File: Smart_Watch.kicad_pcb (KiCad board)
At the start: 4 copper layers, 32 x 32 mm, 59 parts, among them J2 Conn_01x02, J3 Conn_01x06, J4 Conn_01x02, J5 USB_C_Receptacle_USB2.0_16P, SW2 SW_Push, SW3 SW_Push, SW4 SW_Push, SW5 SW_Push, SW6 SW_Push, SW7 SW_Push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

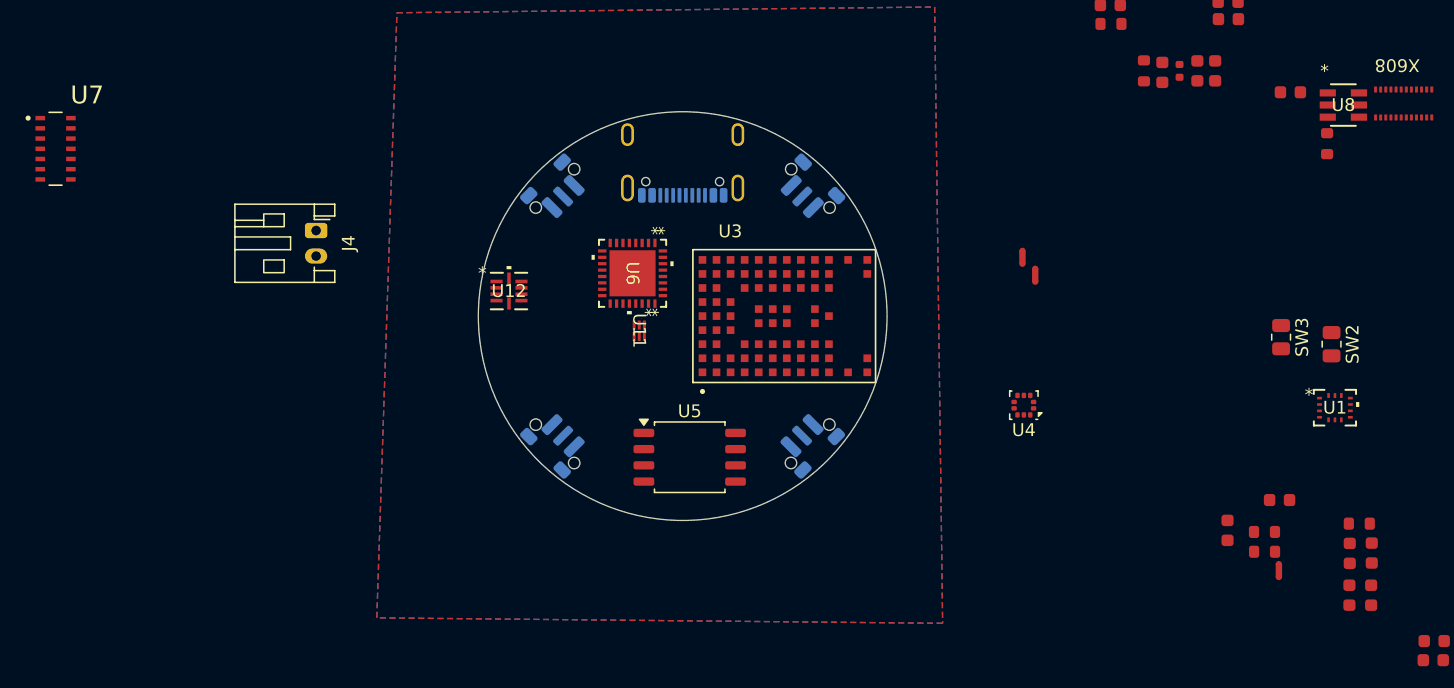
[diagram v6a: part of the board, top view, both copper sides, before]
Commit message: Remove heart rate sensor from main board
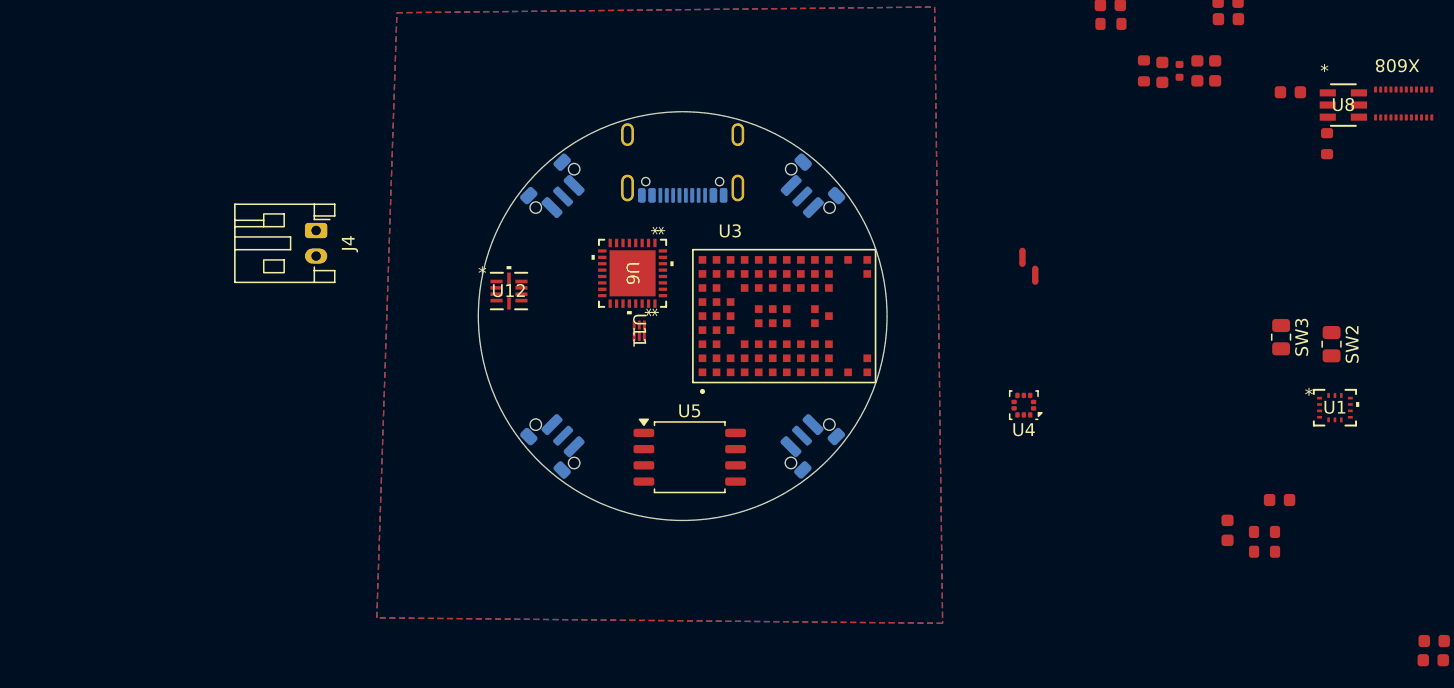
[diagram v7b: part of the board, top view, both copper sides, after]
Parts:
- removed C1: 10uF, PCM_JLCPCB:C_0603
- removed C2, C4: 100nF, PCM_JLCPCB:C_0603
- removed C3: 4.7uF, PCM_JLCPCB:C_0603
- removed NT3: NetTie_2, NetTie:NetTie-2_SMD_Pad0.5mm
- removed R3: 4.7kΩ, PCM_JLCPCB:R_0603
- removed U7: MAX30102EFD_T, Smart_Watch:XDCR_MAX30101EFD_

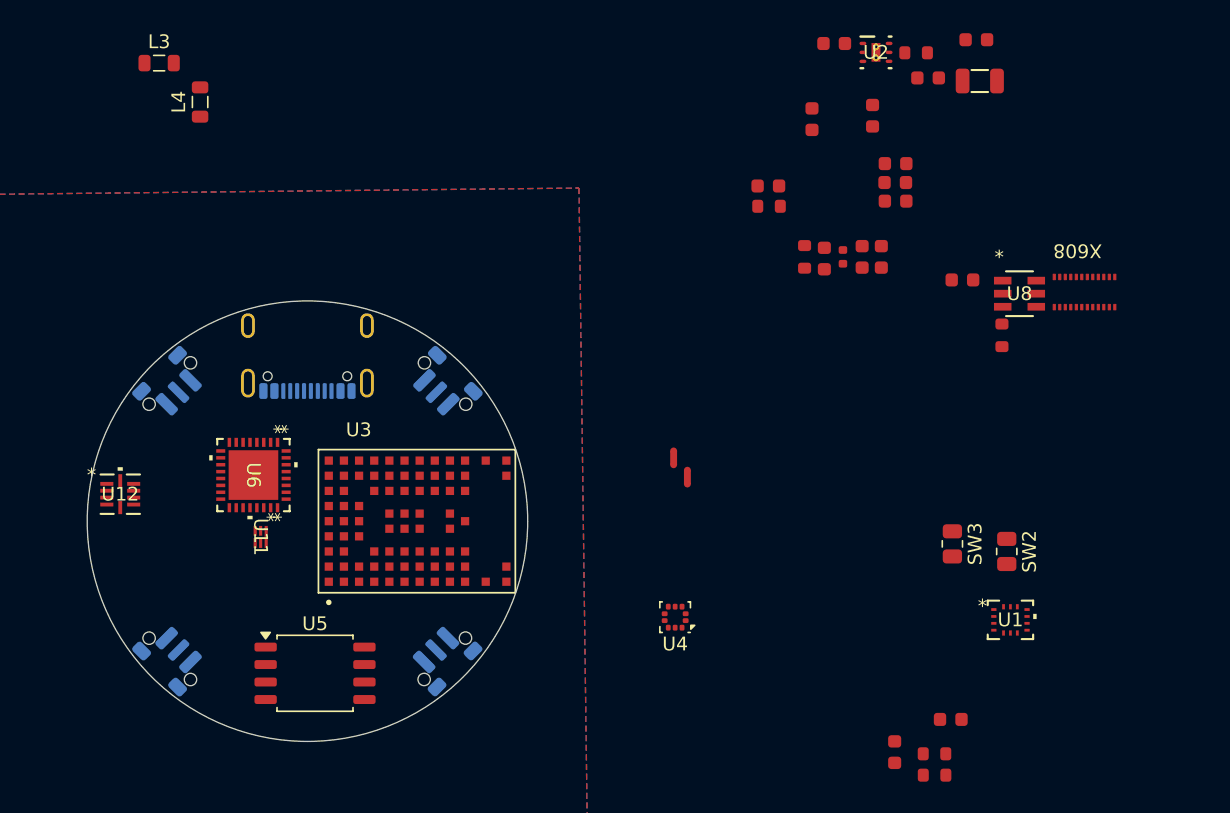
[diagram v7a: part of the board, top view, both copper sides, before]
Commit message: Update the last components and change a couple
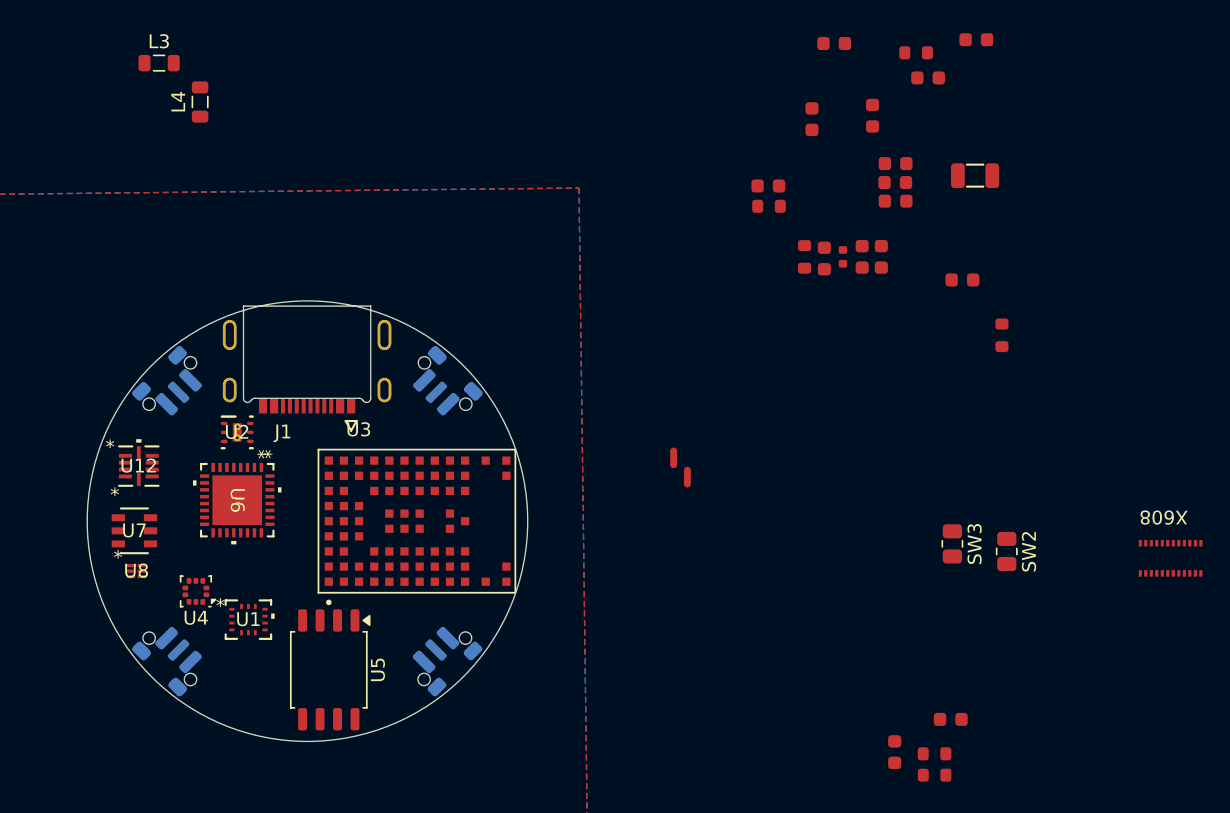
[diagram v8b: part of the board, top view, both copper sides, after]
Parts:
- removed J5: USB_C_Receptacle_USB2.0_16P, Connector_USB:USB_C_Receptacle_GCT_USB4105-xx-A_16P_TopMnt_Horizontal
- removed U11: ESDR0502NMUTBG, ESD:UDFN6_517AA_ONS
- added J1: 2169900001, Smart_Watch:MOLEX_2169900001, F.Cu at (172.1, 92.2)
- added U7: FAN5622SX, Smart_Watch:SSOT6_3X1P7_ONS-L, F.Cu at (159.6, 108.6)
- U8: value FAN5622SX -> ESDR0502NMUTBG; footprint FAN:SSOT6_3X1P7_ONS -> Smart_Watch:UDFN6_517AA_ONS-L
- moved U8 67.2 mm to (159.7, 111.5)
- moved U1 55.4 mm to (167.9, 115.0)
- moved U2 54.0 mm to (167.1, 101.4)
- moved U4 34.9 mm to (164.0, 113.0)
- moved X608 20.3 mm to (234.8, 110.5)
- moved X1 6.88 mm to (220.7, 82.8)
- moved U12 2.45 mm to (159.9, 103.8)
- moved U6 2.17 mm to (167.1, 106.3)
- moved U5 1.03 mm to (173.7, 118.7), turned to -90 degrees
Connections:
- U3 pad A8: unconnected-(U3-VDDH-PadA8) -> /Architecture/MCU/BTN_3
- U3 pad C9: /Architecture/MCU/USBC_D- -> /Architecture/MCU/USBC_D+
- U3 pad D9: unconnected-(U3-USB_DM-PadD9) -> /Architecture/MCU/USBC_D-
- U3 pad H2: unconnected-(U3-SWDIO-PadH2) -> /Architecture/MCU/SWDIO
- U3 pad J2: /Architecture/MCU/SWDIO -> /Architecture/MCU/SWCLK
- U8 pad 1: /Architecture/MCU/DISPLAY_LIGHT_IO -> GND
- U8 pad 2: GND -> unconnected-(U8-NC-Pad2)
- U8 pad 3: +3V0 -> unconnected-(U8-NC-Pad3)
- U8 pad 4: /Architecture/MCU/LEDK2 -> /Architecture/MCU/USBC_D+
- U8 pad 5: /Architecture/MCU/ISET -> /Architecture/MCU/USBC_D-
- U8 pad 6: /Architecture/MCU/LEDK1 -> /Architecture/MCU/VBUS_IN
